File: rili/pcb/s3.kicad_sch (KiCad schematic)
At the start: 1 part, among them U2 ESP32-S3-MINI-1U

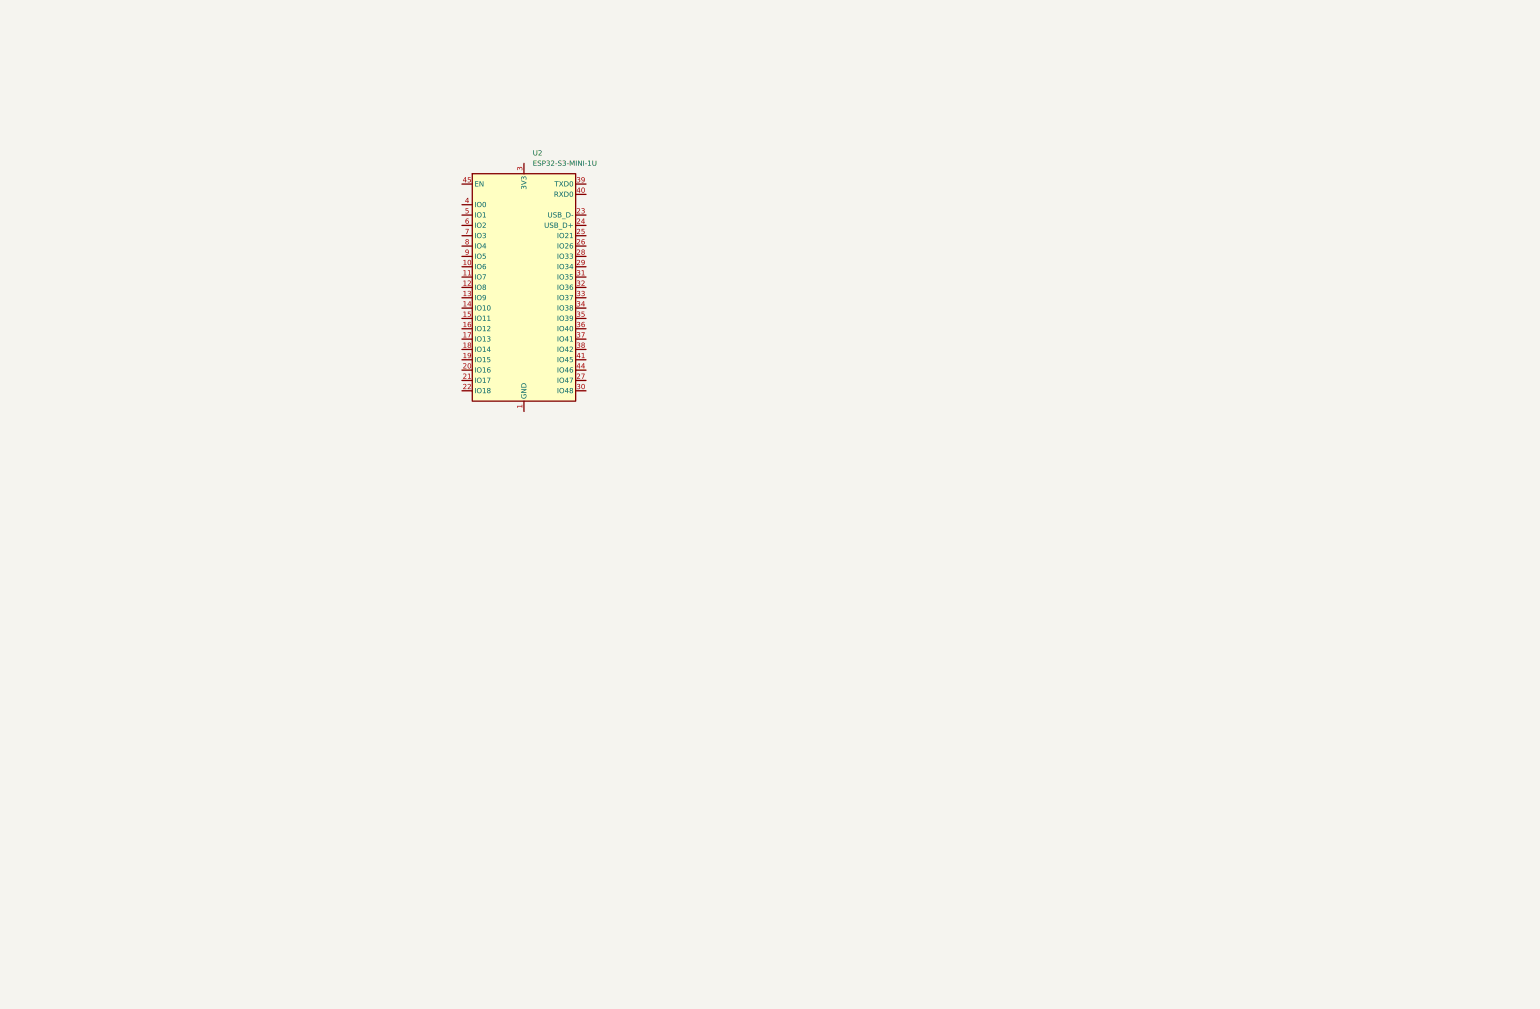
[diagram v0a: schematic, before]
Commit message: WIP schéma v2 Niphargus + rename projet rili → niphar
Grosse session schéma (binôme Mae/Claude) :
- Panneau 2 moitiés : matrice droite miroir, nets séparés (col*_d/row*_d)
- Feuille s3 : ESP32-S3-WROOM-1, matrice 11 GPIO RTC, nRF24 (SPI + 100R),
  J_PROG 6 pins (ESP-Prog), USB_DP/DM, TRRS J6 protégé (SRV05-4 shunt,
  100R série, load switch poignée de main 5V)
- Feuille bat : chaîne 16340 complète — DW01A+FS8205, TP4056 500mA,
  load-sharing AO3407, MCP1700, jauge VBAT_SENSE (validée par netlist)
- Feuille usb : USB-C 16P + CC 5k1 + USBLC6, hub CH334R (S3+P4, mode
  sans crystal, LDO interne isolé du rail 3V3, RESET# pull-up)
- Feuille P4 (coffre, en cours) + Matrix ; hiérarchie intégrée à la racine
- Ménage : fossiles corne-cherry supprimés (rescue.lib conservée, encore
  référencée) ; symbole FS8205 créé ; scripts/mirror_panel.py archivé
- Rename : projet KiCad rili.* → niphar.* (produit « Niphargus »),
  kicad-check.sh et CLAUDE.md retargetés

ERC : 87 erreurs restantes = chantier en cours (pins P4 en attente,
PWR_FLAG, GPIO libres à flagger) — push en connaissance de cause (--no-verify),
baselines à re-référencer quand le schéma sera complet.

Co-Authored-By: Claude Fable 5 <noreply@anthropic.com>
Claude-Session: https://claude.ai/code/session_01GfX5RmekmQi78Dm37qsT4Z
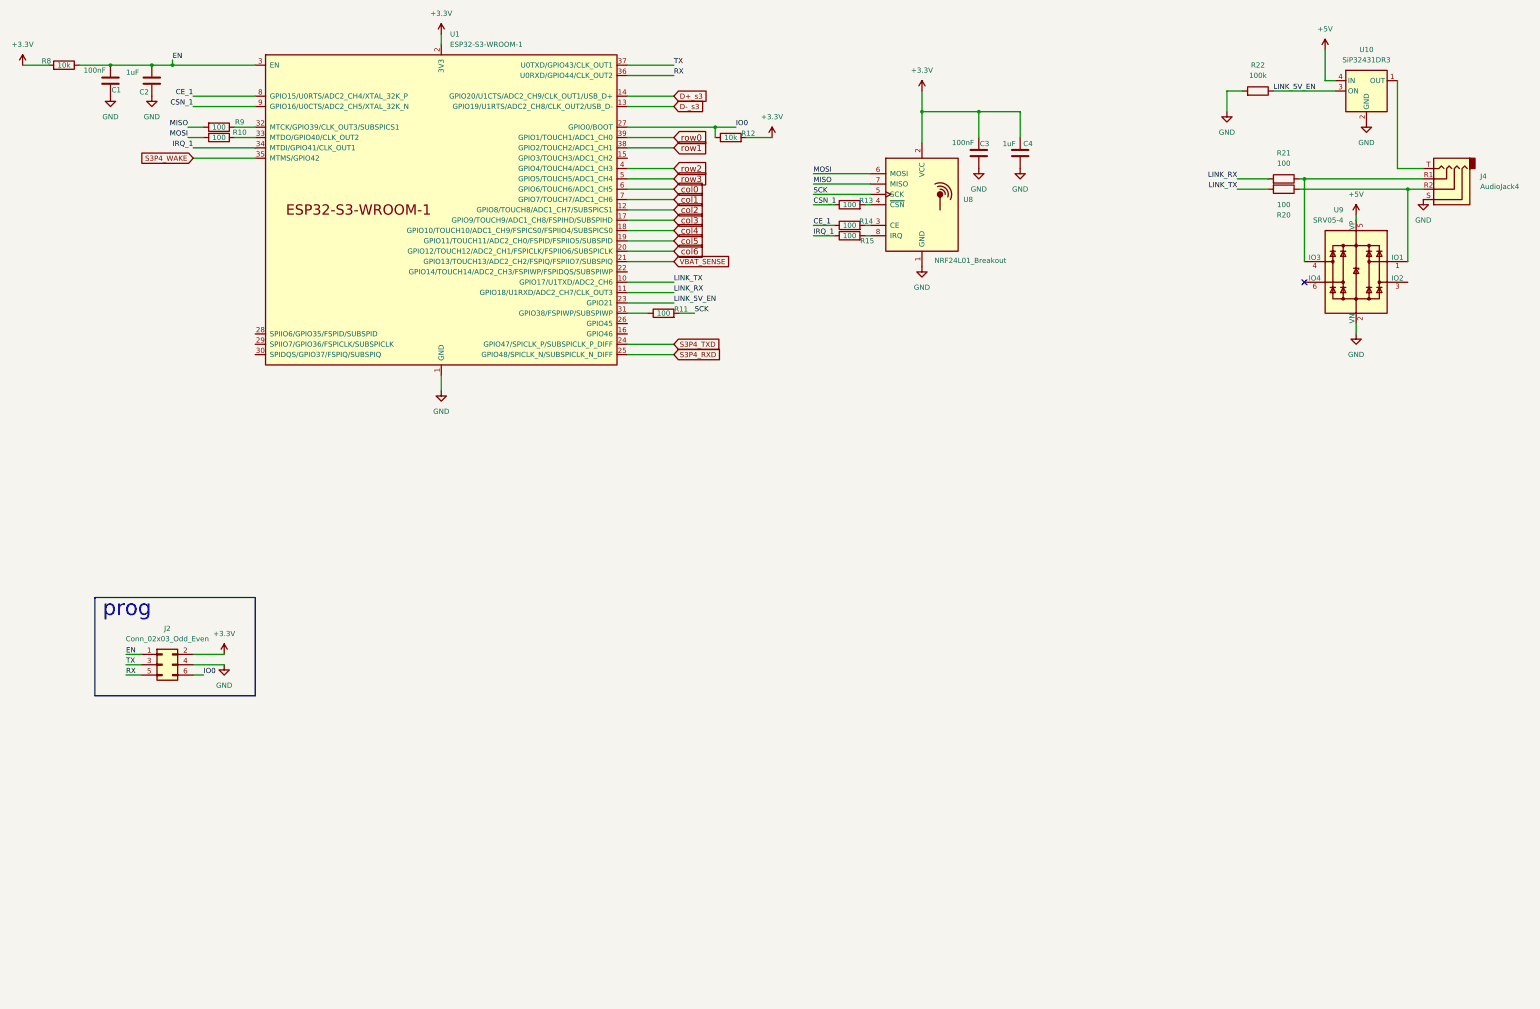
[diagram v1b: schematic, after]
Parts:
- removed U2: ESP32-S3-MINI-1U, RF_Module:ESP32-S2-MINI-1U, symbol RF_Module:ESP32-S3-MINI-1U
- added C1, C3: 100nF, Capacitor_SMD:C_0603_1608Metric, symbol Device:C
- added C2, C4: 1uF, Capacitor_SMD:C_0603_1608Metric, symbol Device:C
- added J2: Conn_02x03_Odd_Even, Connector_PinHeader_1.27mm:PinHeader_2x03_P1.27mm_Vertical, symbol Connector_Generic:Conn_02x03_Odd_Even
- added J4: AudioJack4, symbol Connector_Audio:AudioJack4
- added R10, R11, R13, R14, R15, R9: 100, Resistor_SMD:R_0603_1608Metric, symbol Device:R
- added R12, R8: 10k, Resistor_SMD:R_0603_1608Metric, symbol Device:R
- added R20, R21: 100, Resistor_SMD:R_0603_1608Metric_Pad0.98x0.95mm_HandSolder, symbol Device:R
- added R22: 100k, Resistor_SMD:R_0603_1608Metric_Pad0.98x0.95mm_HandSolder, symbol Device:R
- added U1: ESP32-S3-WROOM-1, PCM_Espressif:ESP32-S3-WROOM-1U, symbol PCM_Espressif:ESP32-S3-WROOM-1
- added U10: SiP32431DR3, Package_TO_SOT_SMD:SOT-363_SC-70-6, symbol Power_Management:SiP32431DR3
- added U8: NRF24L01_Breakout, MaeLid:NRF24L01, symbol RF:NRF24L01_Breakout
- added U9: SRV05-4, Package_TO_SOT_SMD:SOT-23-6, symbol Power_Protection:SRV05-4
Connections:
- new net: J4.R2, R20.1, U9.1 (IO1)
- new net: J4.R1, R21.1, U9.4 (IO3)
- new net: R13.2, U8.4 (~{CSN})
- new net: R11.1, U1.31 (GPIO38/FSPIWP/SUBSPIWP)
- new net: R9.1, U1.32 (MTCK/GPIO39/CLK_OUT3/SUBSPICS1)
- new net: R10.1, U1.33 (MTDO/GPIO40/CLK_OUT2)
- new net: R15.2, U8.8 (IRQ)
- new net: R14.2, U8.3 (CE)
- new net: J4.T, U10.1 (OUT)
- new net +3.3V: C3.2, C4.2, J2.2 (Pin_2), R12.2, R8.2, U1.2 (3V3), U8.2 (VCC)
- new net +5V: U10.4 (IN), U9.5 (VP)
- new net CE_1: R14.1, U1.8 (GPIO15/U0RTS/ADC2_CH4/XTAL_32K_P)
- new net CSN_1: R13.1, U1.9 (GPIO16/U0CTS/ADC2_CH5/XTAL_32K_N)
- new net D+_s3: U1.14 (GPIO20/U1CTS/ADC2_CH9/CLK_OUT1/USB_D+)
- new net D-_s3: U1.13 (GPIO19/U1RTS/ADC2_CH8/CLK_OUT2/USB_D-)
- new net EN: C1.2, C2.2, J2.1 (Pin_1), R8.1, U1.3 (EN)
- new net GND: C1.1, C2.1, C3.1, C4.1, J2.4 (Pin_4), J4.S, R22.2, U1.1 (GND), U1.40 (GND), U1.41 (GND), U10.2 (GND), U10.5 (GND), U8.1 (GND), U9.2 (VN)
- new net IO0: J2.6 (Pin_6), R12.1, U1.27 (GPIO0/BOOT)
- new net IRQ_1: R15.1, U1.34 (MTDI/GPIO41/CLK_OUT1)
- new net LINK_5V_EN: R22.1, U1.23 (GPIO21), U10.3 (ON)
- new net LINK_RX: R21.2, U1.11 (GPIO18/U1RXD/ADC2_CH7/CLK_OUT3)
- new net LINK_TX: R20.2, U1.10 (GPIO17/U1TXD/ADC2_CH6)
- new net MISO: R9.2, U8.7 (MISO)
- new net MOSI: R10.2, U8.6 (MOSI)
- new net RX: J2.5 (Pin_5), U1.36 (U0RXD/GPIO44/CLK_OUT2)
- new net S3P4_RXD: U1.25 (GPIO48/SPICLK_N/SUBSPICLK_N_DIFF)
- new net S3P4_TXD: U1.24 (GPIO47/SPICLK_P/SUBSPICLK_P_DIFF)
- new net S3P4_WAKE: U1.35 (MTMS/GPIO42)
- new net SCK: R11.2, U8.5 (SCK)
- new net TX: J2.3 (Pin_3), U1.37 (U0TXD/GPIO43/CLK_OUT1)
- new net VBAT_SENSE: U1.21 (GPIO13/TOUCH13/ADC2_CH2/FSPIQ/FSPIIO7/SUBSPIQ)
- new net col0: U1.6 (GPIO6/TOUCH6/ADC1_CH5)
- new net col1: U1.7 (GPIO7/TOUCH7/ADC1_CH6)
- new net col2: U1.12 (GPIO8/TOUCH8/ADC1_CH7/SUBSPICS1)
- new net col3: U1.17 (GPIO9/TOUCH9/ADC1_CH8/FSPIHD/SUBSPIHD)
- new net col4: U1.18 (GPIO10/TOUCH10/ADC1_CH9/FSPICS0/FSPIIO4/SUBSPICS0)
- new net col5: U1.19 (GPIO11/TOUCH11/ADC2_CH0/FSPID/FSPIIO5/SUBSPID)
- new net col6: U1.20 (GPIO12/TOUCH12/ADC2_CH1/FSPICLK/FSPIIO6/SUBSPICLK)
- new net row0: U1.39 (GPIO1/TOUCH1/ADC1_CH0)
- new net row1: U1.38 (GPIO2/TOUCH2/ADC1_CH1)
- new net row2: U1.4 (GPIO4/TOUCH4/ADC1_CH3)
- new net row3: U1.5 (GPIO5/TOUCH5/ADC1_CH4)
- no-connect marks 0 -> 1
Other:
- note added: "prog"

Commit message: schéma v2 : coffre P4 complet — ERC 0 erreur
- Feuille p4 (ex sans_titre) : AMS1117-3.3 (rail P4_3V3 séparé, 10µF/22µF),
  CHIP_PU RC 100k+100nF, USB HS (ESP_USB_P/N) vers le port 2 du hub,
  microSD slot UHS-I (CLK/CMD/DAT0-3 sur GPIO39-44, pull-ups 10k),
  prog P4 via port 3 du hub (USB-Serial-JTAG + jumpers d'isolation)
- Périphériques : écran Sharp LS011B7DH03 (SPI partagé, CS_DPL=GPIO14),
  trackpad TPS43 (I2C 47/48, RDY=42, bloc généré+validé), C6 laissé vierge
  (OTA via P4 = voie officielle)
- Ménage ERC : 65 no_connect + 6 PWR_FLAG posés par script (fix_nc.py),
  labels fantômes S3P4 supprimés — ERC projet : 71 → 0 erreur,
  warnings 262 → 158 (ratchet enregistré)
- Hooks Claude Code Stop/PostToolUse désactivés (garde-fou = pre-push + CI)

Reste au schéma : le 2e MCU (moitié droite, col*_d/row*_d en attente).
DRC layout hors périmètre (chantier séparé).

Co-Authored-By: Claude Fable 5 <noreply@anthropic.com>
Claude-Session: https://claude.ai/code/session_01GfX5RmekmQi78Dm37qsT4Z
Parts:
- added C20, C21: 100nF, Capacitor_SMD:C_0603_1608Metric_Pad1.08x0.95mm_HandSolder, symbol Device:C
- added C5: 1uF, Capacitor_SMD:C_0603_1608Metric, symbol Device:C
- added D69, D70, D71, D72, D77, D78, D79, D82, D83, D84, D85, D86, D87, D88, D89, D90, D91, D92, D93, D94, D95, D96, D97, D98, U13, U14: D, EKR82-footprint:Diode_TH_SOD123EKR, symbol Device:D
- added J20: TPS43_FPC, Connector_PinHeader_2.54mm:PinHeader_1x06_P2.54mm_Vertical, symbol Connector_Generic:Conn_01x06
- added J7: Conn_01x05_Pin, Connector_PinHeader_2.54mm:PinHeader_1x05_P2.54mm_Vertical, symbol Connector:Conn_01x05_Pin
- added R35, R36, R37, R38, R39, R40, R41, R42, R43, R44, R45: 100R, Resistor_SMD:R_0603_1608Metric_Pad0.98x0.95mm_HandSolder, symbol Device:R
- added R50, R51: 4.7k, Resistor_SMD:R_0603_1608Metric_Pad0.98x0.95mm_HandSolder, symbol Device:R
- added R52: 100k, Resistor_SMD:R_0603_1608Metric_Pad0.98x0.95mm_HandSolder, symbol Device:R
- added SW100, SW101, SW102, SW103, SW104, SW105, SW74, SW75, SW76, SW77, SW82, SW83, SW84, SW85, SW88, SW89, SW90, SW91, SW92, SW93, SW94, SW95, SW96, SW97, SW98, SW99: SW_PUSH, PMW3360:SW_Hotswap_Kailh_Choc_V1V2_1.00u, symbol corne-cherry-rescue:SW_PUSH-kbd-corne-cherry-rescue
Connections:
- net +3.3V: now also C20.1, C5.2, J20.4 (Pin_4), J7.3 (Pin_3), R50.1, R51.1, R52.1
- net GND: now also C20.2, C21.2, C5.1, J20.3 (Pin_3), J7.4 (Pin_4)
- net MOSI: now also J7.1 (Pin_1)
- net SCK: now also J7.2 (Pin_2)
- net col0: now also R39.2
- net col1: now also R40.2
- net col2: now also R41.2
- net col3: now also R42.2
- net col4: now also R43.2
- net col5: now also R44.2
- net col6: now also R45.2
- net row0: now also R35.1
- net row1: now also R36.1
- net row2: now also R37.1
- net row3: now also R38.1
- net CS_DPL: now reaches U1.22 (GPIO14/TOUCH14/ADC2_CH3/FSPIWP/FSPIDQS/SUBSPIWP)
- net CS_DPL: now also J7.5 (Pin_5)
- net S3P4_RXD renamed TP_SCL
- net TP_SCL: now also J20.5 (Pin_5), R51.2
- net S3P4_TXD renamed TP_SDA
- net TP_SDA: now also J20.6 (Pin_6), R50.2
- net S3P4_WAKE renamed TP_RDY
- net TP_RDY: now also J20.1 (Pin_1)
- new net: D70.1 (K), D78.1 (K), D83.1 (K), D86.1 (K), D90.1 (K), D94.1 (K), D98.1 (K), R36.2
- new net: D70.2 (A), SW75.2
- new net: D72.1 (K), D88.1 (K), D92.1 (K), D96.1 (K), R38.2, U13.1 (K), U14.1 (K)
- new net: R44.1, SW100.1, SW101.1, SW102.1, SW103.1
- new net: D95.2 (A), SW102.2
- new net: D96.2 (A), SW103.2
- new net: R45.1, SW104.1, SW105.1
- new net: R39.1, SW74.1, SW75.1, SW76.1, SW77.1
- new net: D93.2 (A), SW100.2
- new net: SW91.2, U14.2 (A)
- new net: D71.1 (K), D79.1 (K), D84.1 (K), D87.1 (K), D91.1 (K), D95.1 (K), R37.2
- new net: R42.1, SW92.1, SW93.1, SW94.1, SW95.1
- new net: D88.2 (A), SW95.2
- new net: D78.2 (A), SW83.2
- new net: D69.1 (K), D77.1 (K), D82.1 (K), D85.1 (K), D89.1 (K), D93.1 (K), D97.1 (K), R35.2
- new net: D82.2 (A), SW88.2
- new net: D69.2 (A), SW74.2
- new net: D86.2 (A), SW93.2
- new net: R40.1, SW82.1, SW83.1, SW84.1, SW85.1
- new net: D94.2 (A), SW101.2
- new net: R43.1, SW96.1, SW97.1, SW98.1, SW99.1
- new net: D90.2 (A), SW97.2
- new net: R41.1, SW88.1, SW89.1, SW90.1, SW91.1
- new net: D98.2 (A), SW105.2
- new net: D87.2 (A), SW94.2
- new net: D89.2 (A), SW96.2
- new net: D84.2 (A), SW90.2
- new net: D83.2 (A), SW89.2
- new net: D77.2 (A), SW82.2
- new net: SW85.2, U13.2 (A)
- new net: D79.2 (A), SW84.2
- new net: D91.2 (A), SW98.2
- new net: D71.2 (A), SW76.2
- new net: D85.2 (A), SW92.2
- new net: D97.2 (A), SW104.2
- new net: D92.2 (A), SW99.2
- new net: D72.2 (A), SW77.2
- new net TP_NRST: C21.1, J20.2 (Pin_2), R52.2
- no-connect marks 1 -> 8
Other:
- moved on the sheet: C3, C4, J2
